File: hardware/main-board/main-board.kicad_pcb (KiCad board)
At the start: 2 copper layers, 180 x 55 mm, 96 parts, among them J1 BARREL_JACK, J2 CONN_01X10, J3 CONN_01X10, J4 USB_OTG, J5 CONN_02X05, J6 SMA, Q1 DDTD113ZC, Q2 DDTD113ZC, Q3 DDTD113ZC, Q4 DDTD113ZC, Q5 DDTD113ZC, Q6 FDB14N30TM, Q7 DDTD113ZC, Q8 DDTD113ZC, Q9 DDTD113ZC, SW1 SW_Push, SW2 SW_Push, SW3 SW_Push, SW4 SW_Push, U1 LD1117S33TR, U2 MAX1771, U3 STM32F302C, U4 FGPMMOPA6H, Y1 8MHz, Y2 32.768kHz

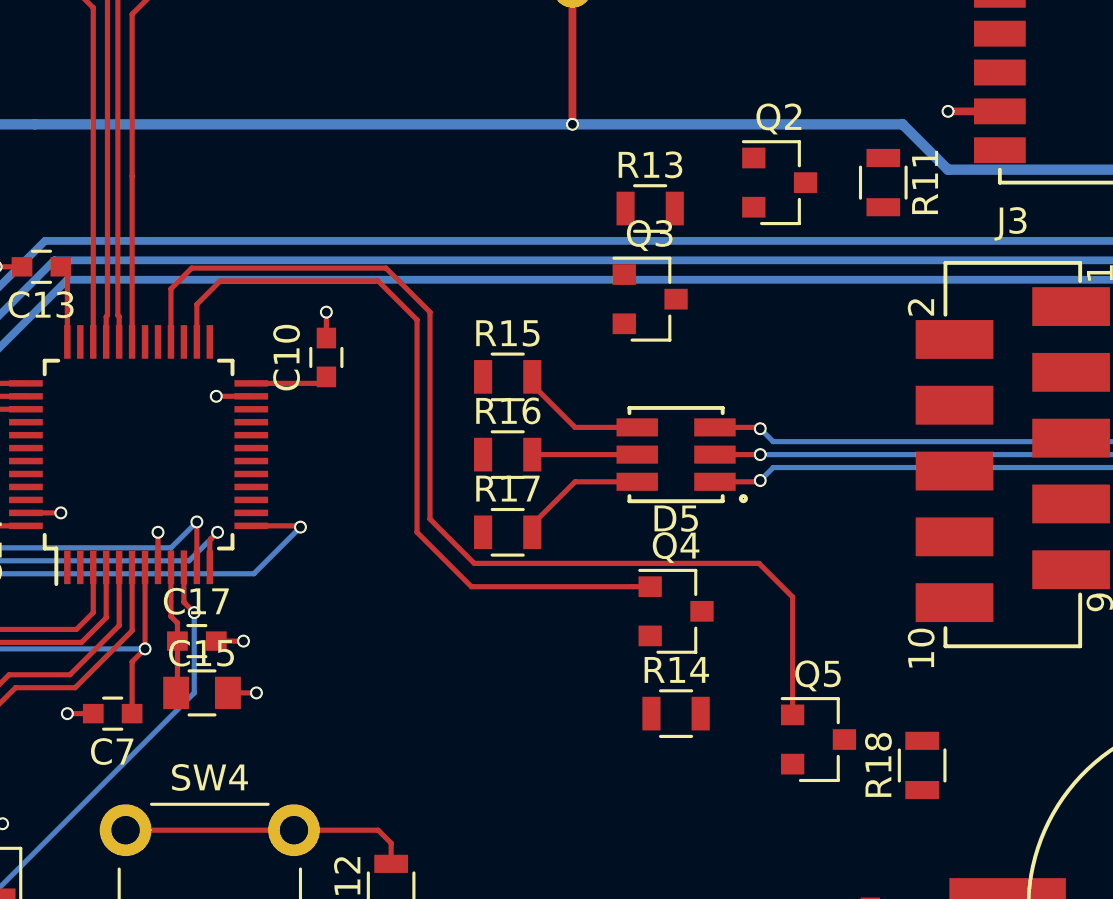
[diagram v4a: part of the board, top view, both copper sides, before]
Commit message: Working on main board layout
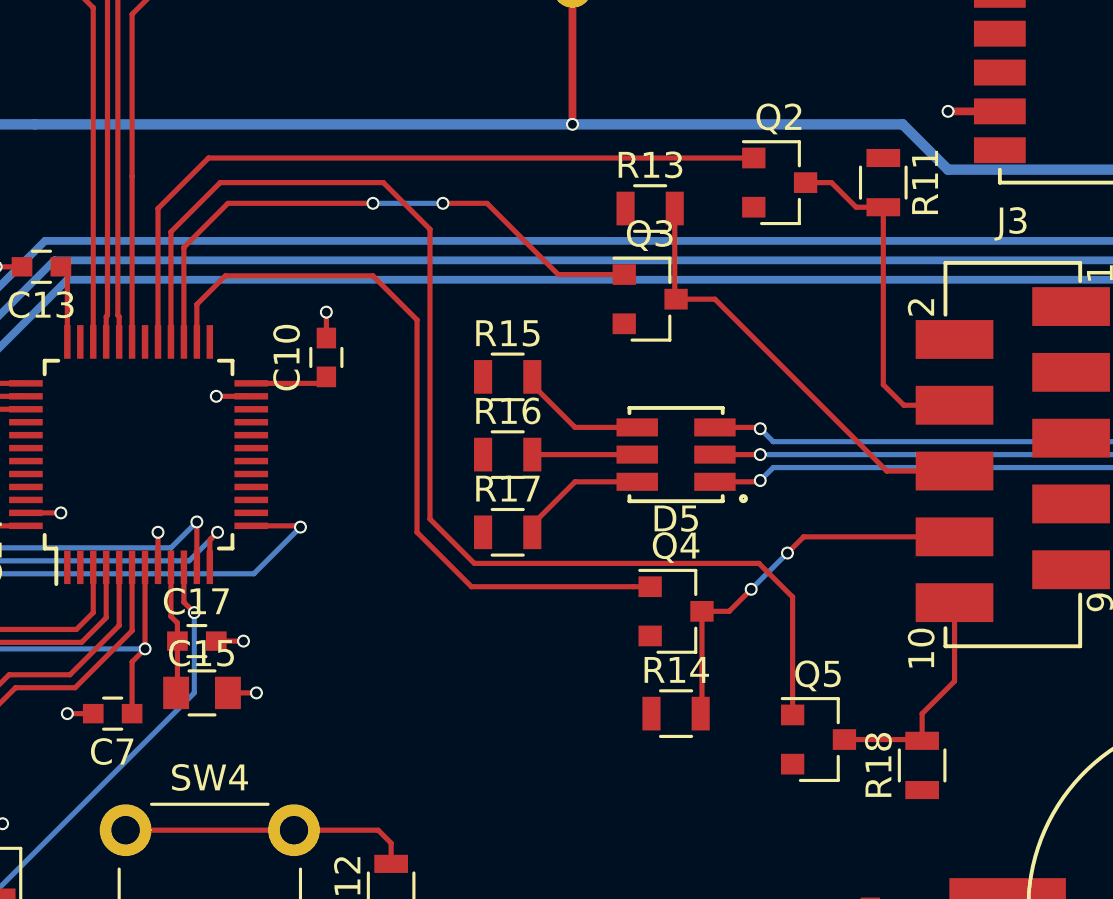
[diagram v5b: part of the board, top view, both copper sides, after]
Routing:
- net /DISP_BL: track 0.00 -> 29.0 mm
- net /DISP_LE: track 0.00 -> 22.5 mm, vias 0 -> 2
- net Net-(J3-Pad6): track 0.00 -> 17.0 mm
- net Net-(J3-Pad8): track 0.00 -> 14.9 mm, vias 0 -> 2
- net Net-(J3-Pad4): track 0.00 -> 13.3 mm
- net Net-(J3-Pad10): track 0.00 -> 8.87 mm
- net /DISP_DATA: track 40.9 -> 46.8 mm
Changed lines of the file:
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@@
 (kicad_pcb (version 4) (host pcbnew 4.0.6)
   (general
-    (links 0)
-    (no_connects 72)
-    (area 59.924999 62.424999 240.075001 117.575001)
+    (links 231)
+    (no_connects 70)
+    (area 52.657143 54.823809 247.342858 120.000001)
     (thickness 1.6)
     (drawings 28)
-    (tracks 590)
+    (tracks 628)
     (zones 0)
     (modules 96)
@@
   )
   (setup
-    (last_trace_width 0.4)
+    (last_trace_width 0.2)
     (user_trace_width 0.3)
     (user_trace_width 0.4)
@@
   (segment (start 110.4 70.5) (end 108.7 70.5) (width 0.8) (layer F.Cu) (net 37))
   (segment (start 105.7 65) (end 105.7 71.1) (width 0.8) (layer F.Cu) (net 37))
+  (segment (start 209.75 88.095) (end 207.795 88.095) (width 0.2) (layer F.Cu) (net 39))
+  (segment (start 207 87.3) (end 207 81) (width 0.2) (layer F.Cu) (net 39))
+  (segment (start 207.795 88.095) (end 207 87.3) (width 0.2) (layer F.Cu) (net 39))
+  (segment (start 207 81) (end 207 80.45) (width 0.2) (layer F.Cu) (net 39))
+  (segment (start 204 79.5) (end 205 79.5) (width 0.2) (layer F.Cu) (net 39))
+  (segment (start 205 79.5) (end 205.95 80.45) (width 0.2) (layer F.Cu) (net 39))
+  (segment (start 205.95 80.45) (end 207 80.45) (width 0.2) (layer F.Cu) (net 39))
+  (segment (start 198.95 80.5) (end 198.95 83.95) (width 0.2) (layer F.Cu) (net 40))
+  (segment (start 198.95 83.95) (end 199 84) (width 0.2) (layer F.Cu) (net 40))
+  (segment (start 209.75 90.635) (end 207.135 90.635) (width 0.2) (layer F.Cu) (net 40))
+  (segment (start 207.135 90.635) (end 200.5 84) (width 0.2) (layer F.Cu) (net 40))
+  (segment (start 200.5 84) (end 199 84) (width 0.2) (layer F.Cu) (net 40))
+  (segment (start 200 96.05) (end 200 99.95) (width 0.2) (layer F.Cu) (net 41))
+  (segment (start 200 99.95) (end 199.95 100) (width 0.2) (layer F.Cu) (net 41))
+  (segment (start 203.3 93.8) (end 203.925 93.175) (width 0.2) (layer F.Cu) (net 41))
+  (segment (start 203.925 93.175) (end 209.75 93.175) (width 0.2) (layer F.Cu) (net 41))
+  (segment (start 201.9 95.2) (end 203.3 93.8) (width 0.2) (layer B.Cu) (net 41))
+  (via (at 203.3 93.8) (size 0.5) (drill 0.34) (layers F.Cu B.Cu) (net 41))
+  (segment (start 200 96.05) (end 201.05 96.05) (width 0.2) (layer F.Cu) (net 41))
+  (segment (start 201.05 96.05) (end 201.9 95.2) (width 0.2) (layer F.Cu) (net 41))
+  (via (at 201.9 95.2) (size 0.5) (drill 0.34) (layers F.Cu B.Cu) (net 41))
+  (segment (start 205.5 101) (end 208.45 101) (width 0.2) (layer F.Cu) (net 42))
+  (segment (start 208.45 101) (end 208.5 101.05) (width 0.2) (layer F.Cu) (net 42))
+  (segment (start 209.75 95.715) (end 209.75 98.75) (width 0.2) (layer F.Cu) (net 42))
+  (segment (start 209.75 98.75) (end 208.5 100) (width 0.2) (layer F.Cu) (net 42))
+  (segment (start 208.5 100) (end 208.5 101.05) (width 0.2) (layer F.Cu) (net 42))
   (segment (start 178.8 71) (end 178.8 72.2) (width 0.2) (layer F.Cu) (net 43))
   (segment (start 178.8 72.2) (end 178 73) (width 0.2) (layer F.Cu) (net 43))
@@
   (via (at 97.5 101) (size 0.5) (drill 0.34) (layers F.Cu B.Cu) (net 58))
   (via (at 91.5 97.25) (size 0.5) (drill 0.34) (layers F.Cu B.Cu) (net 58))
+  (segment (start 180.95 78.55) (end 179 80.5) (width 0.2) (layer F.Cu) (net 59))
+  (segment (start 179 80.5) (end 179 85.65) (width 0.2) (layer F.Cu) (net 59))
+  (segment (start 202 78.55) (end 180.95 78.55) (width 0.2) (layer F.Cu) (net 59))
+  (segment (start 180 85.65) (end 180 82) (width 0.2) (layer F.Cu) (net 60))
+  (segment (start 180 82) (end 181.7 80.3) (width 0.2) (layer F.Cu) (net 60))
+  (segment (start 181.7 80.3) (end 187.3 80.3) (width 0.2) (layer F.Cu) (net 60))
+  (segment (start 190 80.3) (end 191.7 80.3) (width 0.2) (layer F.Cu) (net 60))
+  (segment (start 191.7 80.3) (end 194.45 83.05) (width 0.2) (layer F.Cu) (net 60))
+  (segment (start 194.45 83.05) (end 197 83.05) (width 0.2) (layer F.Cu) (net 60))
+  (segment (start 187.3 80.3) (end 190 80.3) (width 0.2) (layer B.Cu) (net 60))
+  (via (at 190 80.3) (size 0.5) (drill 0.34) (layers F.Cu B.Cu) (net 60))
+  (via (at 187.3 80.3) (size 0.5) (drill 0.34) (layers F.Cu B.Cu) (net 60))
   (segment (start 180.5 85.65) (end 180.5 84.2) (width 0.2) (layer F.Cu) (net 61))
-  (segment (start 180.5 84.2) (end 181.4 83.3) (width 0.2) (layer F.Cu) (net 61))
-  (segment (start 181.4 83.3) (end 187.5 83.3) (width 0.2) (layer F.Cu) (net 61))
-  (segment (start 189 93) (end 191.1 95.1) (width 0.2) (layer F.Cu) (net 61))
-  (segment (start 187.5 83.3) (end 189 84.8) (width 0.2) (layer F.Cu) (net 61))
+  (segment (start 180.5 84.2) (end 181.6 83.1) (width 0.2) (layer F.Cu) (net 61))
+  (segment (start 181.6 83.1) (end 187.3 83.1) (width 0.2) (layer F.Cu) (net 61))
+  (segment (start 187.3 83.1) (end 189 84.8) (width 0.2) (layer F.Cu) (net 61))
   (segment (start 189 84.8) (end 189 93) (width 0.2) (layer F.Cu) (net 61))
+  (segment (start 189 93) (end 191.1 95.1) (width 0.2) (layer F.Cu) (net 61))
   (segment (start 191.1 95.1) (end 197.35 95.1) (width 0.2) (layer F.Cu) (net 61))
   (segment (start 197.35 95.1) (end 198 95.1) (width 0.2) (layer F.Cu) (net 61))
-  (segment (start 179.5 85.65) (end 179.5 83.6) (width 0.2) (layer F.Cu) (net 62))
-  (segment (start 179.5 83.6) (end 180.3 82.8) (width 0.2) (layer F.Cu) (net 62))
-  (segment (start 187.8 82.8) (end 189.5 84.5) (width 0.2) (layer F.Cu) (net 62))
-  (segment (start 180.3 82.8) (end 187.8 82.8) (width 0.2) (layer F.Cu) (net 62))
-  (segment (start 189.5 84.5) (end 189.5 92.490002) (width 0.2) (layer F.Cu) (net 62))
+  (segment (start 179.5 85.65) (end 179.5 81.4) (width 0.2) (layer F.Cu) (net 62))
+  (segment (start 187.7 79.5) (end 189.5 81.3) (width 0.2) (layer F.Cu) (net 62))
+  (segment (start 179.5 81.4) (end 181.4 79.5) (width 0.2) (layer F.Cu) (net 62))
+  (segment (start 181.4 79.5) (end 187.7 79.5) (width 0.2) (layer F.Cu) (net 62))
+  (segment (start 202.2 94.2) (end 203.5 95.5) (width 0.2) (layer F.Cu) (net 62))
+  (segment (start 189.5 81.3) (end 189.5 92.490002) (width 0.2) (layer F.Cu) (net 62))
   (segment (start 189.5 92.490002) (end 191.209998 94.2) (width 0.2) (layer F.Cu) (net 62))
   (segment (start 191.209998 94.2) (end 202.2 94.2) (width 0.2) (layer F.Cu) (net 62))
-  (segment (start 202.2 94.2) (end 203.5 95.5) (width 0.2) (layer F.Cu) (net 62))
   (segment (start 203.5 95.5) (end 203.5 100.05) (width 0.2) (layer F.Cu) (net 62))
   (segment (start 78.7 104.7) (end 79.3 105.3) (width 0.2) (layer F.Cu) (net 63))

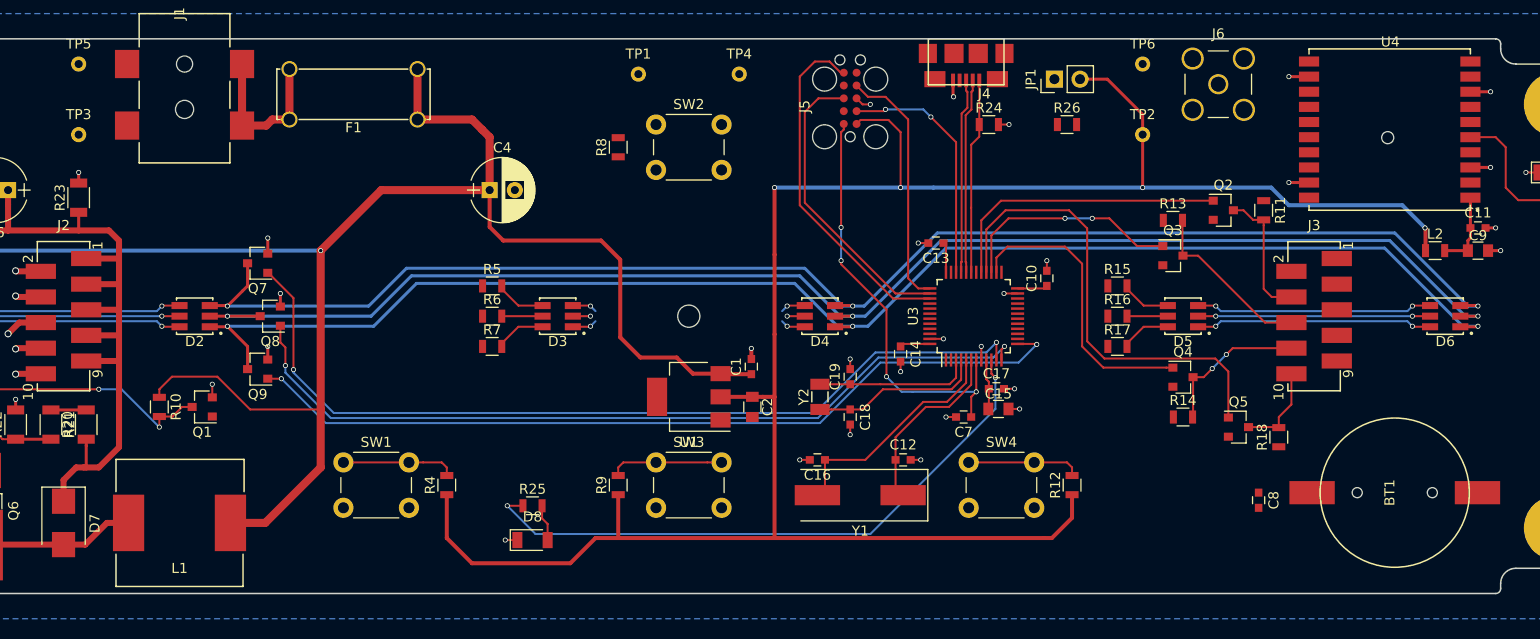
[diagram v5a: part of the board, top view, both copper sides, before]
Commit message: Working on main board layout
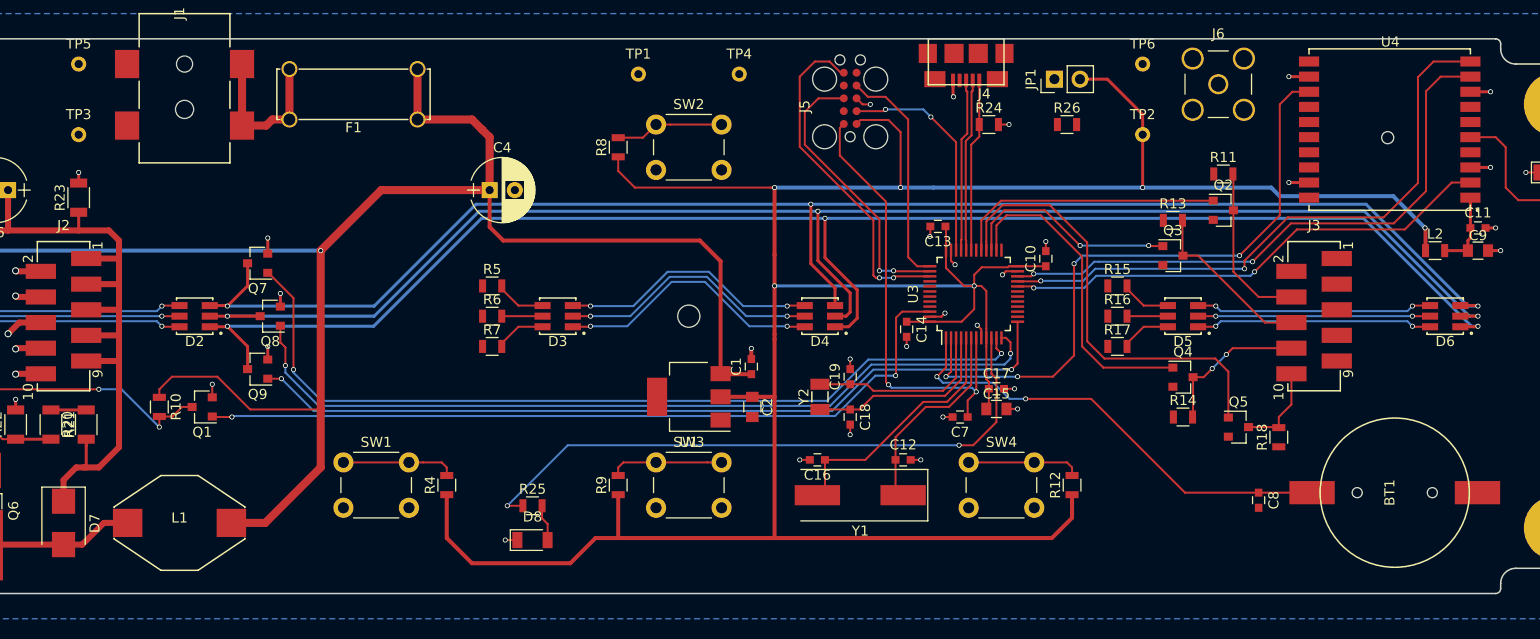
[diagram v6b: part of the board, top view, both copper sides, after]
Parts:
- L1: footprint radio-clock:B82477R4104M100 -> radio-clock:DO3316P
- moved R11 5.38 mm to (203.0, 75.9), turned to 0 degrees
- moved C14 2.52 mm to (171.6, 91.3)
- moved U3 2.20 mm to (178.2, 87.8)
- moved C10 1.95 mm to (185.4, 84.3)
- moved C13 1.66 mm to (174.7, 81.1)
- moved C7 0.35 mm to (176.9, 100.0)
- moved C15 0.20 mm to (180.5, 99.2)
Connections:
- U3 pad 25: /HV_EN -> Net-(U3-Pad25)
- U3 pad 46: Net-(U3-Pad46) -> /HV_EN
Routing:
- net /HV_EN: track 0.00 -> 78.8 mm, vias 0 -> 2
- net /GPS_PPS: track 0.00 -> 63.5 mm, vias 0 -> 4
- net +3V3: track 223.7 -> 286.2 mm, vias 4 -> 6
- net /GPS_RX: track 0.00 -> 60.5 mm, vias 0 -> 2
- net /GPS_TX: track 0.00 -> 58.9 mm, vias 0 -> 2
- net /GPS_RESET: track 0.00 -> 49.3 mm, vias 0 -> 2
- net Net-(BT1-Pad1): track 0.00 -> 46.2 mm, vias 0 -> 2
- net Net-(D3-Pad2): track 3.50 -> 26.2 mm
- net Net-(D3-Pad1): track 4.96 -> 26.7 mm
- net Net-(D3-Pad3): track 4.96 -> 25.9 mm
- net Net-(D2-Pad1): track 144.3 -> 155.3 mm
- net /PB4: track 0.00 -> 10.8 mm
- net Net-(D2-Pad2): track 142.0 -> 152.4 mm
- net Net-(D2-Pad3): track 143.5 -> 152.0 mm
- net Net-(J3-Pad4): track 13.3 -> 16.5 mm
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
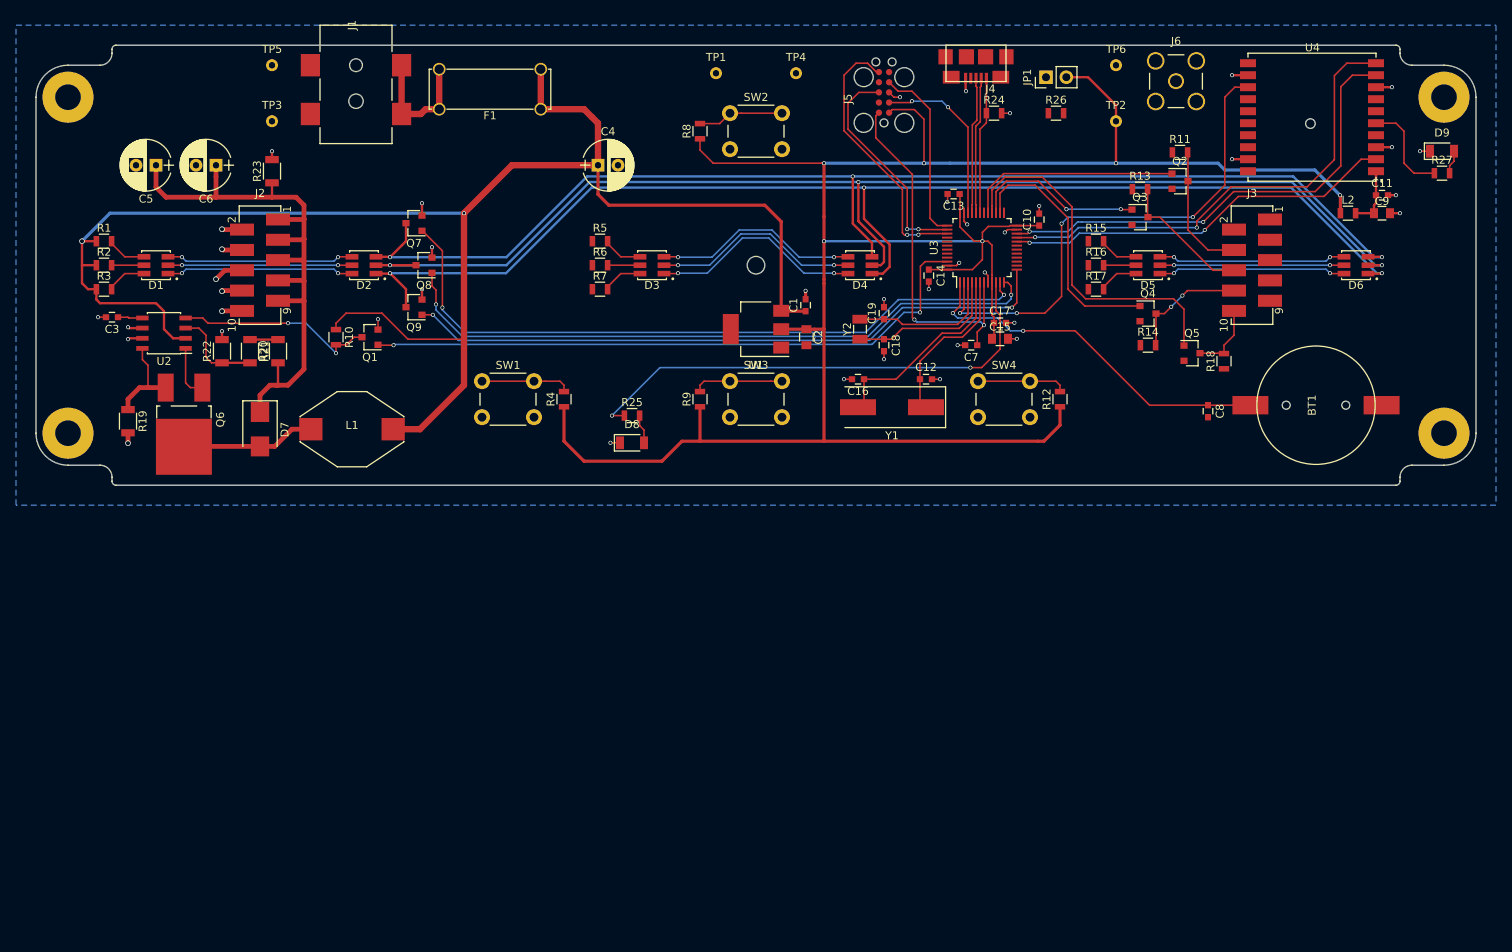
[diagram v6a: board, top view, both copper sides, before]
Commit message: Working on main board layout
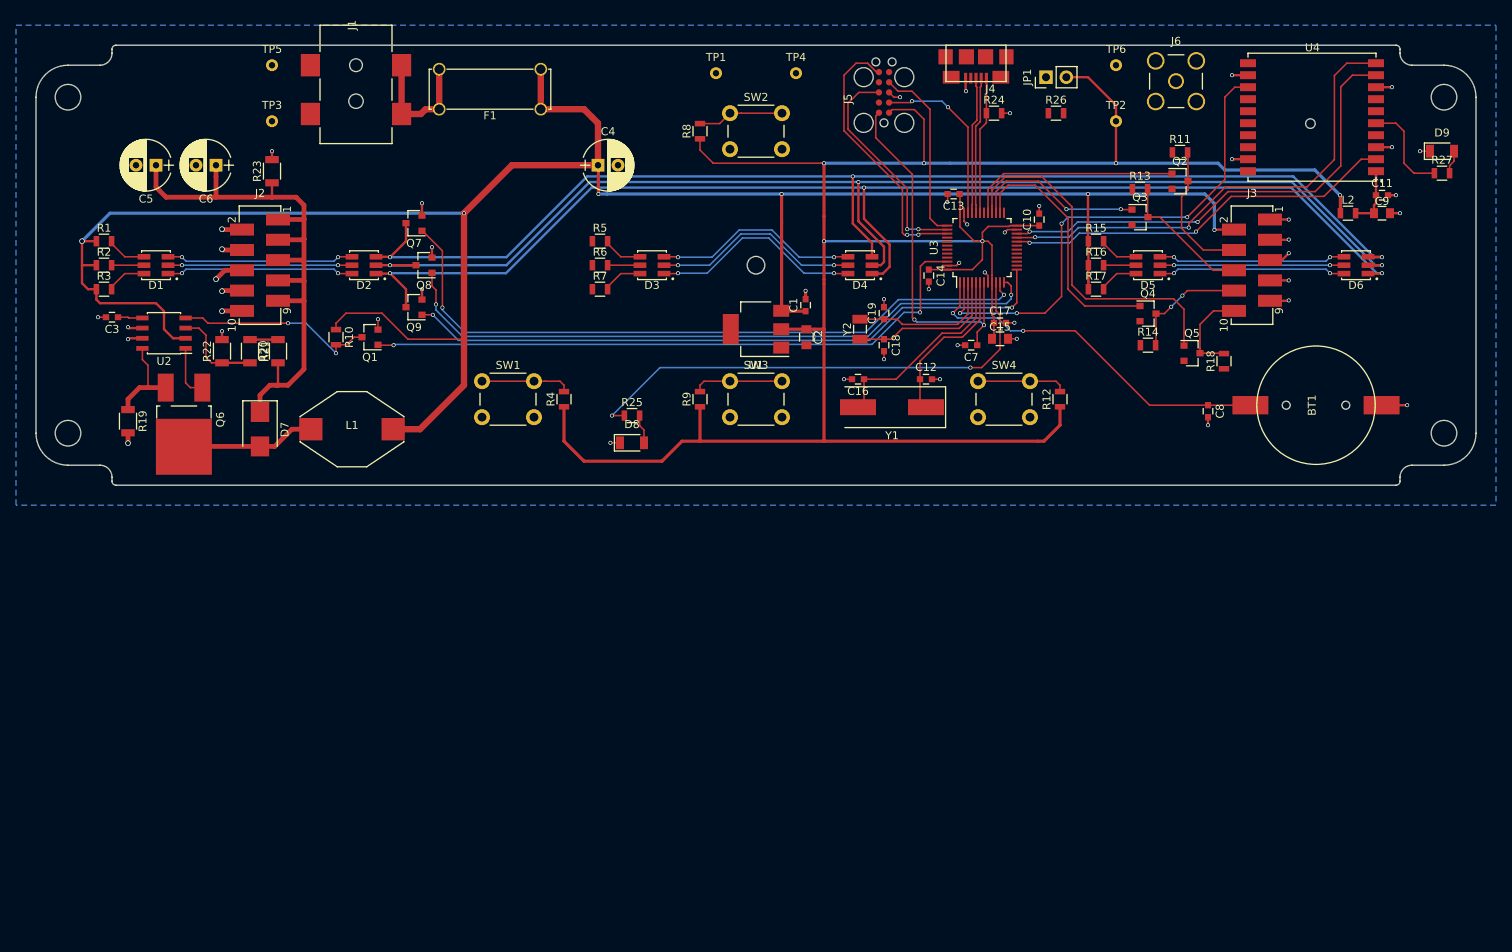
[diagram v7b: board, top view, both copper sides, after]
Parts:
- REF** (x4): footprint Mounting_Holes:MountingHole_3.2mm_M3_Pad -> Mounting_Holes:MountingHole_3.2mm_M3
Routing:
- net +12V: track 206.8 -> 281.1 mm, vias 2 -> 6
- net GND: track 61.8 -> 78.1 mm, vias 41 -> 48
- net Net-(J3-Pad10): track 8.87 -> 11.6 mm
- net Net-(J3-Pad4): track 16.5 -> 17.5 mm
